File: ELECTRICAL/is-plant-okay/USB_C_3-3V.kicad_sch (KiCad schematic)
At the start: 0 parts

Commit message: feat: add usb and esd protection device
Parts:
- added C11: 4n7 1KV, symbol Device:C
- added J7: USB4085-GF-A_REVB, is-plant-okay-foot:GCT_USB4085-GF-A_REVB, symbol is-plant-okay-lib:USB4085-GF-A_REVB
- added R12: 1M, symbol Device:R
- added R13, R14: 5.1k, symbol Device:R
- added U6: USBLC6-2SC6, is-plant-okay-foot:SOT95P280X145-6N, symbol is-plant-okay-lib:USBLC6-2SC6
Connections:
- new net: J7.A5 (CC1), R14.2
- new net: J7.B5 (CC2), R13.2
- new net: C11.1, J7.S1 (SHELL), J7.S2 (SHELL__1), J7.S3 (SHELL__2), J7.S4 (SHELL__3), R12.1
- new net 5V: J7.A4 (VBUS), J7.A9 (VBUS__1), J7.B4 (VBUS__2), J7.B9 (VBUS__3), U6.5
- new net DATA_NEG: J7.A7 (DN1), J7.B7 (DN2), U6.3
- new net DATA_POS: J7.A6 (DP1), J7.B6 (DP2), U6.1
- new net GND: C11.2, J7.A1 (GND), J7.A12 (GND__1), J7.B1 (GND__2), J7.B12 (GND__3), R12.2, R13.1, R14.1, U6.2
- no-connect marks 0 -> 4

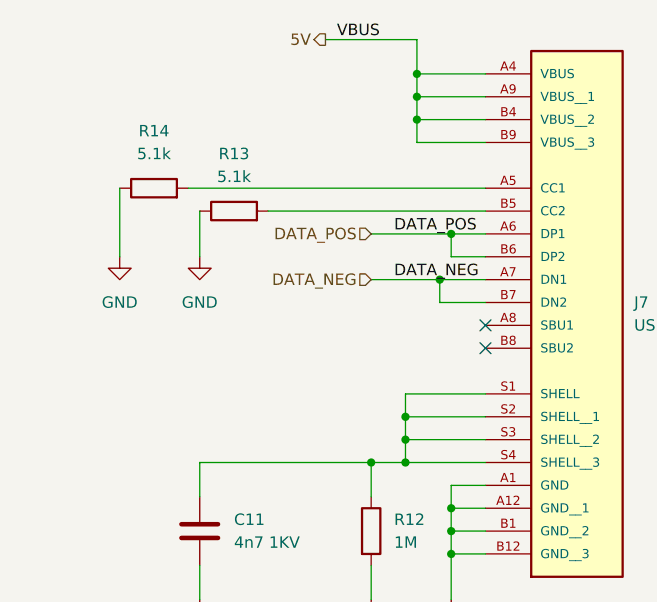
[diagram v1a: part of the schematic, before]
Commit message: feat: add ldo and power management IC
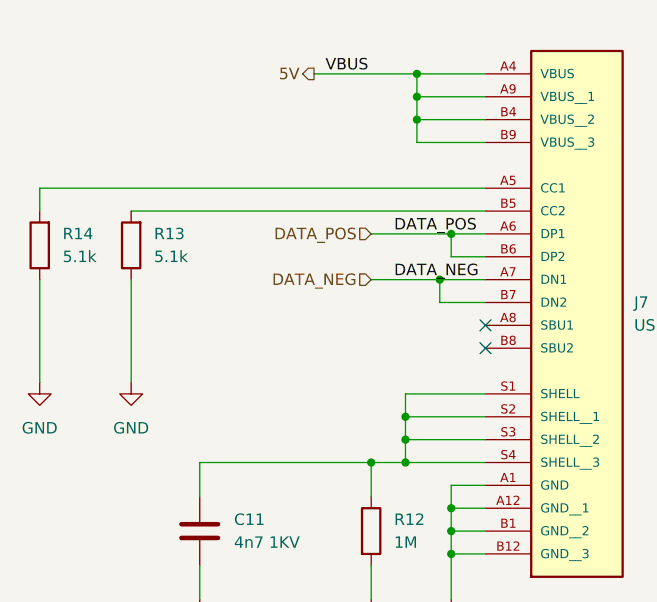
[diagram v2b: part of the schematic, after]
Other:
- moved on the sheet: R13, R14
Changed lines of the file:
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@@
 	(wire
 		(pts
-			(xy 99.06 80.01) (xy 99.06 85.09)
+			(xy 91.44 87.63) (xy 91.44 99.06)
 		)
 		(stroke
@@
 	(wire
 		(pts
-			(xy 97.79 77.47) (xy 130.81 77.47)
-		)
-		(stroke
-			(width 0)
-			(type default)
-		)
-	)
-	(wire
-		(pts
 			(xy 118.11 87.63) (xy 125.73 87.63)
 		)
@@
 	(wire
 		(pts
+			(xy 81.28 77.47) (xy 81.28 80.01)
+		)
+		(stroke
+			(width 0)
+			(type default)
+		)
+	)
+	(wire
+		(pts
 			(xy 127 118.11) (xy 127 123.19)
 		)
@@
 	(wire
 		(pts
-			(xy 106.68 80.01) (xy 130.81 80.01)
-		)
-		(stroke
-			(width 0)
-			(type default)
-		)
-	)
-	(wire
-		(pts
 			(xy 99.06 107.95) (xy 99.06 111.76)
 		)
@@
 	(wire
 		(pts
-			(xy 123.19 64.77) (xy 123.19 60.96)
-		)
-		(stroke
-			(width 0)
-			(type default)
-		)
-	)
-	(wire
-		(pts
 			(xy 127 110.49) (xy 127 113.03)
 		)
@@
 	(wire
 		(pts
-			(xy 113.03 60.96) (xy 123.19 60.96)
+			(xy 111.76 64.77) (xy 123.19 64.77)
 		)
 		(stroke
@@
 	(wire
 		(pts
+			(xy 81.28 77.47) (xy 130.81 77.47)
+		)
+		(stroke
+			(width 0)
+			(type default)
+		)
+	)
+	(wire
+		(pts
 			(xy 127 113.03) (xy 127 115.57)
 		)
@@
 	(wire
 		(pts
-			(xy 90.17 77.47) (xy 90.17 85.09)
-		)
-		(stroke
-			(width 0)
-			(type default)
-		)
-	)
-	(wire
-		(pts
 			(xy 123.19 69.85) (xy 130.81 69.85)
 		)
@@
 	(wire
 		(pts
+			(xy 81.28 87.63) (xy 81.28 99.06)
+		)
+		(stroke
+			(width 0)
+			(type default)
+		)
+	)
+	(wire
+		(pts
 			(xy 125.73 87.63) (xy 130.81 87.63)
 		)
@@
 	(wire
 		(pts
+			(xy 91.44 80.01) (xy 130.81 80.01)
+		)
+		(stroke
+			(width 0)
+			(type default)
+		)
+	)
+	(wire
+		(pts
 			(xy 121.92 100.33) (xy 121.92 102.87)
 		)
@@
 	)
 	(label "VBUS"
-		(at 114.3 60.96 0)
+		(at 113.03 64.77 0)
 		(effects
 			(font
@@
 	(hierarchical_label "5V"
 		(shape output)
-		(at 113.03 60.96 180)
+		(at 111.76 64.77 180)
 		(effects
 			(font
@@
 	(symbol
 		(lib_id "power:GND")
-		(at 90.17 85.09 0)
+		(at 81.28 99.06 0)
 		(unit 1)
 		(exclude_from_sim no)
@@
 		(fields_autoplaced yes)
 		(property "Reference" "#PWR036"
-			(at 90.17 91.44 0)
+			(at 81.28 105.41 0)
 			(effects
 				(font
@@
 		)
 		(property "Value" "GND"
-			(at 90.17 90.17 0)
+			(at 81.28 104.14 0)
 			(effects
 				(font
@@
 		)
 		(property "Footprint" ""
-			(at 90.17 85.09 0)
+			(at 81.28 99.06 0)
 			(effects
 				(font
@@
 		)
 		(property "Datasheet" ""
-			(at 90.17 85.09 0)
+			(at 81.28 99.06 0)
 			(effects
 				(font
@@
 		)
 		(property "Description" "Power symbol creates a global label with name \"GND\" , ground"
-			(at 90.17 85.09 0)
+			(at 81.28 99.06 0)
 			(effects
 				(font
@@
 	(symbol
 		(lib_id "Device:R")
-		(at 102.87 80.01 90)
+		(at 91.44 83.82 180)
 		(unit 1)
 		(exclude_from_sim no)
@@
 		(fields_autoplaced yes)
 		(property "Reference" "R13"
-			(at 102.87 73.66 90)
-			(effects
-				(font
-					(size 1.27 1.27)
-				)
+			(at 93.98 82.5499 0)
+			(effects
+				(font
+					(size 1.27 1.27)
+				)
+				(justify right)
 			)
 		)
 		(property "Value" "5.1k"
-			(at 102.87 76.2 90)
-			(effects
-				(font
-					(size 1.27 1.27)
-				)
+			(at 93.98 85.0899 0)
+			(effects
+				(font
+					(size 1.27 1.27)
+				)
+				(justify right)
 			)
 		)
 		(property "Footprint" ""
-			(at 102.87 81.788 90)
+			(at 93.218 83.82 90)
 			(effects
 				(font
@@
 		)
 		(property "Datasheet" "~"
-			(at 102.87 80.01 0)
+			(at 91.44 83.82 0)
 			(effects
 				(font
@@
 		)
 		(property "Description" "Resistor"
-			(at 102.87 80.01 0)
+			(at 91.44 83.82 0)
 			(effects
 				(font
@@
 	(symbol
 		(lib_id "power:GND")
-		(at 99.06 85.09 0)
+		(at 91.44 99.06 0)
 		(unit 1)
 		(exclude_from_sim no)
@@
 		(fields_autoplaced yes)
 		(property "Reference" "#PWR035"
-			(at 99.06 91.44 0)
+			(at 91.44 105.41 0)
 			(effects
 				(font
@@
 		)
 		(property "Value" "GND"
-			(at 99.06 90.17 0)
+			(at 91.44 104.14 0)
 			(effects
 				(font
@@
 		)
 		(property "Footprint" ""
-			(at 99.06 85.09 0)
+			(at 91.44 99.06 0)
 			(effects
 				(font
@@
 		)
 		(property "Datasheet" ""
-			(at 99.06 85.09 0)
+			(at 91.44 99.06 0)
 			(effects
 				(font
@@
 		)
 		(property "Description" "Power symbol creates a global label with name \"GND\" , ground"
-			(at 99.06 85.09 0)
+			(at 91.44 99.06 0)
 			(effects
 				(font
@@
 	(symbol
 		(lib_id "Device:R")
-		(at 93.98 77.47 90)
+		(at 81.28 83.82 180)
 		(unit 1)
 		(exclude_from_sim no)
@@
 		(fields_autoplaced yes)
 		(property "Reference" "R14"
-			(at 93.98 71.12 90)
-			(effects
-				(font
-					(size 1.27 1.27)
-				)
+			(at 83.82 82.5499 0)
+			(effects
+				(font
+					(size 1.27 1.27)
+				)
+				(justify right)
 			)
 		)
 		(property "Value" "5.1k"
-			(at 93.98 73.66 90)
-			(effects
-				(font
-					(size 1.27 1.27)
-				)
+			(at 83.82 85.0899 0)
+			(effects
+				(font
+					(size 1.27 1.27)
+				)
+				(justify right)
 			)
 		)
 		(property "Footprint" ""
-			(at 93.98 79.248 90)
+			(at 83.058 83.82 90)
 			(effects
 				(font
@@
 		)
 		(property "Datasheet" "~"
-			(at 93.98 77.47 0)
+			(at 81.28 83.82 0)
 			(effects
 				(font
@@
 		)
 		(property "Description" "Resistor"
-			(at 93.98 77.47 0)
-			(effects
-				(font
+			(at 81.28 83.82 0)
+			(effects
+				(font

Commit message: feat: add ldo and power management IC
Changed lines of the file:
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@@
+	)
+	(junction
+		(at 120.65 64.77)
+		(diameter 0)
+		(color 0 0 0 0)
 	)
 	(junction
@@
 	(junction
 		(at 123.19 67.31)
+		(diameter 0)
+		(color 0 0 0 0)
+	)
+	(junction
+		(at 127 125.73)
 		(diameter 0)
 		(color 0 0 0 0)
@@
 	(wire
 		(pts
+			(xy 120.65 64.77) (xy 123.19 64.77)
+		)
+		(stroke
+			(width 0)
+			(type default)
+		)
+	)
+	(wire
+		(pts
 			(xy 127 113.03) (xy 130.81 113.03)
 		)
@@
 	(wire
 		(pts
-			(xy 127 118.11) (xy 127 123.19)
+			(xy 127 118.11) (xy 127 125.73)
 		)
 		(stroke
@@
 	(wire
 		(pts
-			(xy 99.06 119.38) (xy 99.06 123.19)
+			(xy 99.06 119.38) (xy 99.06 127)
 		)
 		(stroke
@@
 	(wire
 		(pts
-			(xy 111.76 64.77) (xy 123.19 64.77)
+			(xy 111.76 64.77) (xy 120.65 64.77)
 		)
 		(stroke
@@
 	(wire
 		(pts
-			(xy 118.11 119.38) (xy 118.11 123.19)
+			(xy 118.11 119.38) (xy 118.11 127)
 		)
 		(stroke
@@
 		(pts
 			(xy 121.92 107.95) (xy 130.81 107.95)
+		)
+		(stroke
+			(width 0)
+			(type default)
+		)
+	)
+	(wire
+		(pts
+			(xy 127 125.73) (xy 127 127)
 		)
 		(stroke
@@
 	)
 	(symbol
+		(lib_id "power:PWR_FLAG")
+		(at 127 125.73 270)
+		(unit 1)
+		(exclude_from_sim no)
+		(in_bom yes)
+		(on_board yes)
+		(dnp no)
+		(fields_autoplaced yes)
+		(property "Reference" "#FLG02"
+			(at 128.905 125.73 0)
+			(effects
+				(font
+					(size 1.27 1.27)
+				)
+				(hide yes)
+			)
+		)
+		(property "Value" "PWR_FLAG"
+			(at 130.81 125.7299 90)
+			(effects
+				(font
+					(size 1.27 1.27)
+				)
+				(justify left)
+			)
+		)
+		(property "Footprint" ""
+			(at 127 125.73 0)
+			(effects
+				(font
+					(size 1.27 1.27)
+				)
+				(hide yes)
+			)
+		)
+		(property "Datasheet" "~"
+			(at 127 125.73 0)
+			(effects
+				(font
+					(size 1.27 1.27)
+				)
+				(hide yes)
+			)
+		)
+		(property "Description" "Special symbol for telling ERC where power comes from"
+			(at 127 125.73 0)
+			(effects
+				(font
+					(size 1.27 1.27)
+				)
+				(hide yes)
+			)
+		)
+		(pin "1"
+		)
+		(instances
+			(project "is-plant-okay"
+				(path "/ac51c2f9-77a4-4b89-b63f-6e0ba02b1e45/67cc056f-c5be-4963-a238-c27ae3faab2e"
+					(reference "#FLG02")
+					(unit 1)
+				)
+			)
+		)
+	)
+	(symbol
 		(lib_id "power:GND")
-		(at 99.06 123.19 0)
+		(at 99.06 127 0)
 		(unit 1)
 		(exclude_from_sim no)
@@
 		(fields_autoplaced yes)
 		(property "Reference" "#PWR034"
-			(at 99.06 129.54 0)
+			(at 99.06 133.35 0)
 			(effects
 				(font
@@
 		)
 		(property "Value" "GND"
-			(at 99.06 128.27 0)
+			(at 99.06 132.08 0)
 			(effects
 				(font
@@
 		)
 		(property "Footprint" ""
-			(at 99.06 123.19 0)
+			(at 99.06 127 0)
 			(effects
 				(font
@@
 		)
 		(property "Datasheet" ""
-			(at 99.06 123.19 0)
+			(at 99.06 127 0)
 			(effects
 				(font
@@
 		)
 		(property "Description" "Power symbol creates a global label with name \"GND\" , ground"
-			(at 99.06 123.19 0)
+			(at 99.06 127 0)
 			(effects
 				(font
@@
 				(path "/ac51c2f9-77a4-4b89-b63f-6e0ba02b1e45/67cc056f-c5be-4963-a238-c27ae3faab2e"
 					(reference "#PWR034")
+					(unit 1)
+				)
+			)
+		)
+	)
+	(symbol
+		(lib_id "power:PWR_FLAG")
+		(at 120.65 64.77 0)
+		(unit 1)
+		(exclude_from_sim no)
+		(in_bom yes)
+		(on_board yes)
+		(dnp no)
+		(fields_autoplaced yes)
+		(property "Reference" "#FLG01"
+			(at 120.65 62.865 0)
+			(effects
+				(font
+					(size 1.27 1.27)
+				)
+				(hide yes)
+			)
+		)
+		(property "Value" "PWR_FLAG"
+			(at 120.65 59.69 0)
+			(effects
+				(font
+					(size 1.27 1.27)
+				)
+			)
+		)
+		(property "Footprint" ""
+			(at 120.65 64.77 0)
+			(effects
+				(font
+					(size 1.27 1.27)
+				)
+				(hide yes)
+			)
+		)
+		(property "Datasheet" "~"
+			(at 120.65 64.77 0)
+			(effects
+				(font
+					(size 1.27 1.27)
+				)
+				(hide yes)
+			)
+		)
+		(property "Description" "Special symbol for telling ERC where power comes from"
+			(at 120.65 64.77 0)
+			(effects
+				(font
+					(size 1.27 1.27)
+				)
+				(hide yes)
+			)
+		)
+		(pin "1"
+		)
+		(instances
+			(project ""
+				(path "/ac51c2f9-77a4-4b89-b63f-6e0ba02b1e45/67cc056f-c5be-4963-a238-c27ae3faab2e"
+					(reference "#FLG01")
 					(unit 1)
 				)
@@
 	(symbol
 		(lib_id "power:GND")
-		(at 127 123.19 0)
+		(at 127 127 0)
 		(unit 1)
 		(exclude_from_sim no)
@@
 		(fields_autoplaced yes)
 		(property "Reference" "#PWR032"
-			(at 127 129.54 0)
+			(at 127 133.35 0)
 			(effects
 				(font
@@
 		)
 		(property "Value" "GND"
-			(at 127 128.27 0)
+			(at 127 132.08 0)
 			(effects
 				(font
@@
 		)
 		(property "Footprint" ""
-			(at 127 123.19 0)
+			(at 127 127 0)
 			(effects
 				(font
@@
 		)
 		(property "Datasheet" ""
-			(at 127 123.19 0)
+			(at 127 127 0)
 			(effects
 				(font
@@
 		)
 		(property "Description" "Power symbol creates a global label with name \"GND\" , ground"
-			(at 127 123.19 0)
+			(at 127 127 0)
 			(effects
 				(font
@@
 	(symbol
 		(lib_id "power:GND")
-		(at 118.11 123.19 0)
+		(at 118.11 127 0)
 		(unit 1)
 		(exclude_from_sim no)
@@
 		(fields_autoplaced yes)
 		(property "Reference" "#PWR033"
-			(at 118.11 129.54 0)
+			(at 118.11 133.35 0)
 			(effects
 				(font
@@
 		)
 		(property "Value" "GND"
-			(at 118.11 128.27 0)
+			(at 118.11 132.08 0)
 			(effects
 				(font
@@
 		)
 		(property "Footprint" ""
-			(at 118.11 123.19 0)
+			(at 118.11 127 0)
 			(effects
 				(font
@@
 		)
 		(property "Datasheet" ""
-			(at 118.11 123.19 0)
+			(at 118.11 127 0)
 			(effects
 				(font
@@
 		)
 		(property "Description" "Power symbol creates a global label with name \"GND\" , ground"
-			(at 118.11 123.19 0)
-			(effects
-				(font
+			(at 118.11 127 0)
+			(effects
+				(font

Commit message: feat: add pins for bootloader programmer
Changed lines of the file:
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@@
 	)
 	(hierarchical_label "DATA_NEG"
-		(shape input)
+		(shape output)
 		(at 118.11 87.63 180)
 		(effects
@@
 	)
 	(hierarchical_label "DATA_POS"
-		(shape input)
+		(shape output)
 		(at 118.11 82.55 180)
 		(effects

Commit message: feat: finished schematics
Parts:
- added TP8: USB_5V_TP, TestPoint:TestPoint_Keystone_5000-5004_Miniature, symbol Connector:TestPoint
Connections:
- net 5V: now also TP8.1
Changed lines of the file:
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@@
+	)
+	(junction
+		(at 96.52 64.77)
+		(diameter 0)
+		(color 0 0 0 0)
 	)
 	(junction
@@
 	(wire
 		(pts
+			(xy 96.52 64.77) (xy 120.65 64.77)
+		)
+		(stroke
+			(width 0)
+			(type default)
+		)
+	)
+	(wire
+		(pts
 			(xy 127 118.11) (xy 127 125.73)
 		)
@@
 	(wire
 		(pts
-			(xy 111.76 64.77) (xy 120.65 64.77)
+			(xy 93.98 64.77) (xy 96.52 64.77)
 		)
 		(stroke
@@
 	(hierarchical_label "5V"
 		(shape output)
-		(at 111.76 64.77 180)
+		(at 93.98 64.77 180)
 		(effects
 			(font
@@
 					(unit 1)
 				)
+			)
+		)
+	)
+	(symbol
+		(lib_id "Connector:TestPoint")
+		(at 96.52 64.77 0)
+		(unit 1)
+		(exclude_from_sim no)
+		(in_bom yes)
+		(on_board yes)
+		(dnp no)
+		(fields_autoplaced yes)
+		(property "Reference" "TP8"
+			(at 99.06 60.1979 0)
+			(effects
+				(font
+					(size 1.27 1.27)
+				)
+				(justify left)
+			)
+		)
+		(property "Value" "USB_5V_TP"
+			(at 99.06 62.7379 0)
+			(effects
+				(font
+					(size 1.27 1.27)
+				)
+				(justify left)
+			)
+		)
+		(property "Footprint" "TestPoint:TestPoint_Keystone_5000-5004_Miniature"
+			(at 101.6 64.77 0)
+			(effects
+				(font
+					(size 1.27 1.27)
+				)
+				(hide yes)
+			)
+		)
+		(property "Datasheet" "~"
+			(at 101.6 64.77 0)
+			(effects
+				(font
+					(size 1.27 1.27)
+				)
+				(hide yes)
+			)
+		)
+		(property "Description" "test point"
+			(at 96.52 64.77 0)
+			(effects
+				(font
+					(size 1.27 1.27)
+				)
+				(hide yes)
+			)
+		)
+		(pin "1"
+		)
+		(instances
+			(project "is-plant-okay"
+				(path "/ac51c2f9-77a4-4b89-b63f-6e0ba02b1e45/67cc056f-c5be-4963-a238-c27ae3faab2e"
+					(reference "TP8")
+					(unit 1)
+				)

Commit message: feat: add resistor footprint
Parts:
- removed R12: 1M, symbol Device:R
- removed R13, R14: 5.1k, symbol Device:R
- added R1, R2: 5.1k, is-plant-okay-foot:RC0805JR-075K1L, symbol Device:R
- added R3: 10K, is-plant-okay-foot:RC0805FR-7W10KL, symbol Device:R
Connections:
- net GND: now also R1.1, R2.1, R3.2
- net at J7.A5 (CC1): now also R1.2
- net at J7.B5 (CC2): now also R2.2
- net at C11.1, J7.S1 (SHELL), J7.S2 (SHELL__1)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: now also R3.1
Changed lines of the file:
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@@
+	)
+	(symbol
+		(lib_id "Device:R")
+		(at 118.11 115.57 0)
+		(unit 1)
+		(exclude_from_sim no)
+		(in_bom yes)
+		(on_board yes)
+		(dnp no)
+		(fields_autoplaced yes)
+		(property "Reference" "R3"
+			(at 120.65 114.2999 0)
+			(effects
+				(font
+					(size 1.27 1.27)
+				)
+				(justify left)
+			)
+		)
+		(property "Value" "10K"
+			(at 120.65 116.8399 0)
+			(effects
+				(font
+					(size 1.27 1.27)
+				)
+				(justify left)
+			)
+		)
+		(property "Footprint" "is-plant-okay-foot:RC0805FR-7W10KL"
+			(at 116.332 115.57 90)
+			(effects
+				(font
+					(size 1.27 1.27)
+				)
+				(hide yes)
+			)
+		)
+		(property "Datasheet" "~https://www.yageogroup.com/content/datasheet/asset/file/PYU-RC_GROUP_51_ROHS_L"
+			(at 118.11 115.57 0)
+			(effects
+				(font
+					(size 1.27 1.27)
+				)
+				(hide yes)
+			)
+		)
+		(property "Description" "RES 10K OHM 1% 1/4W 0805"
+			(at 118.11 115.57 0)
+			(effects
+				(font
+					(size 1.27 1.27)
+				)
+				(hide yes)
+			)
+		)
+		(property "MFG PART #" "RC0805FR-7W10KL"
+			(at 118.11 115.57 0)
+			(effects
+				(font
+					(size 1.27 1.27)
+				)
+				(hide yes)
+			)
+		)
+		(property "TYPE" "SMD"
+			(at 118.11 115.57 0)
+			(effects
+				(font
+					(size 1.27 1.27)
+				)
+				(hide yes)
+			)
+		)
+		(property "PACKAGE" "0805"
+			(at 118.11 115.57 0)
+			(effects
+				(font
+					(size 1.27 1.27)
+				)
+				(hide yes)
+			)
+		)
+		(pin "1"
+		)
+		(pin "2"
+		)
+		(instances
+			(project "is-plant-okay"
+				(path "/ac51c2f9-77a4-4b89-b63f-6e0ba02b1e45/67cc056f-c5be-4963-a238-c27ae3faab2e"
+					(reference "R3")
+					(unit 1)
+				)
+			)
+		)
 	)
 	(symbol
@@
 	)
 	(symbol
+		(lib_id "Device:R")
+		(at 91.44 83.82 180)
+		(unit 1)
+		(exclude_from_sim no)
+		(in_bom yes)
+		(on_board yes)
+		(dnp no)
+		(fields_autoplaced yes)
+		(property "Reference" "R2"
+			(at 93.98 82.5499 0)
+			(effects
+				(font
+					(size 1.27 1.27)
+				)
+				(justify right)
+			)
+		)
+		(property "Value" "5.1k"
+			(at 93.98 85.0899 0)
+			(effects
+				(font
+					(size 1.27 1.27)
+				)
+				(justify right)
+			)
+		)
+		(property "Footprint" "is-plant-okay-foot:RC0805JR-075K1L"
+			(at 93.218 83.82 90)
+			(effects
+				(font
+					(size 1.27 1.27)
+				)
+				(hide yes)
+			)
+		)
+		(property "Datasheet" "https://www.yageogroup.com/content/datasheet/asset/file/PYU-RC_GROUP_51_ROHS_L"
+			(at 91.44 83.82 0)
+			(effects
+				(font
+					(size 1.27 1.27)
+				)
+				(hide yes)
+			)
+		)
+		(property "Description" "RES 5.1K OHM 5% 1/8W 0805"
+			(at 91.44 83.82 0)
+			(effects
+				(font
+					(size 1.27 1.27)
+				)
+				(hide yes)
+			)
+		)
+		(property "MFG PART #" "RC0805JR-075K1L"
+			(at 91.44 83.82 0)
+			(effects
+				(font
+					(size 1.27 1.27)
+				)
+				(hide yes)
+			)
+		)
+		(property "TYPE" "SMD"
+			(at 91.44 83.82 0)
+			(effects
+				(font
+					(size 1.27 1.27)
+				)
+				(hide yes)
+			)
+		)
+		(property "PACKAGE" "0805"
+			(at 91.44 83.82 0)
+			(effects
+				(font
+					(size 1.27 1.27)
+				)
+				(hide yes)
+			)
+		)
+		(pin "1"
+		)
+		(pin "2"
+		)
+		(instances
+			(project "is-plant-okay"
+				(path "/ac51c2f9-77a4-4b89-b63f-6e0ba02b1e45/67cc056f-c5be-4963-a238-c27ae3faab2e"
+					(reference "R2")
+					(unit 1)
+				)
+			)
+		)
+	)
+	(symbol
 		(lib_id "power:GND")
 		(at 81.28 99.06 0)
@@
 	)
 	(symbol
-		(lib_id "Device:R")
-		(at 91.44 83.82 180)
-		(unit 1)
-		(exclude_from_sim no)
-		(in_bom yes)
-		(on_board yes)
-		(dnp no)
-		(fields_autoplaced yes)
-		(property "Reference" "R13"
-			(at 93.98 82.5499 0)
-			(effects
-				(font
-					(size 1.27 1.27)
-				)
-				(justify right)
-			)
-		)
-		(property "Value" "5.1k"
-			(at 93.98 85.0899 0)
-			(effects
-				(font
-					(size 1.27 1.27)
-				)
-				(justify right)
-			)
-		)
-		(property "Footprint" ""
-			(at 93.218 83.82 90)
-			(effects
-				(font
-					(size 1.27 1.27)
-				)
-				(hide yes)
-			)
-		)
-		(property "Datasheet" "~"
-			(at 91.44 83.82 0)
-			(effects
-				(font
-					(size 1.27 1.27)
-				)
-				(hide yes)
-			)
-		)
-		(property "Description" "Resistor"
-			(at 91.44 83.82 0)
-			(effects
-				(font
-					(size 1.27 1.27)
-				)
-				(hide yes)
-			)
-		)
-		(pin "1"
-		)
-		(pin "2"
-		)
-		(instances
-			(project "is-plant-okay"
-				(path "/ac51c2f9-77a4-4b89-b63f-6e0ba02b1e45/67cc056f-c5be-4963-a238-c27ae3faab2e"
-					(reference "R13")
-					(unit 1)
-				)
-			)
-		)
-	)
-	(symbol
 		(lib_id "power:GND")
 		(at 91.44 99.06 0)
@@
 	(symbol
 		(lib_id "Device:R")
-		(at 118.11 115.57 0)
-		(unit 1)
-		(exclude_from_sim no)
-		(in_bom yes)
-		(on_board yes)
-		(dnp no)
-		(fields_autoplaced yes)
-		(property "Reference" "R12"
-			(at 120.65 114.2999 0)
-			(effects
-				(font
-					(size 1.27 1.27)
-				)
-				(justify left)
-			)
-		)
-		(property "Value" "1M"
-			(at 120.65 116.8399 0)
-			(effects
-				(font
-					(size 1.27 1.27)
-				)
-				(justify left)
-			)
-		)
-		(property "Footprint" ""
-			(at 116.332 115.57 90)
-			(effects
-				(font
-					(size 1.27 1.27)
-				)
-				(hide yes)
-			)
-		)
-		(property "Datasheet" "~"
-			(at 118.11 115.57 0)
-			(effects
-				(font
-					(size 1.27 1.27)
-				)
-				(hide yes)
-			)
-		)
-		(property "Description" "Resistor"
-			(at 118.11 115.57 0)
-			(effects
-				(font
-					(size 1.27 1.27)
-				)
-				(hide yes)
-			)
-		)
-		(pin "1"
-		)
-		(pin "2"
-		)
-		(instances
-			(project ""
-				(path "/ac51c2f9-77a4-4b89-b63f-6e0ba02b1e45/67cc056f-c5be-4963-a238-c27ae3faab2e"
-					(reference "R12")
-					(unit 1)
-				)
-			)
-		)
-	)
-	(symbol
-		(lib_id "Device:R")
 		(at 81.28 83.82 180)
 		(unit 1)
@@
 		(dnp no)
 		(fields_autoplaced yes)
-		(property "Reference" "R14"
+		(property "Reference" "R1"
 			(at 83.82 82.5499 0)
 			(effects
@@
 			)
 		)
-		(property "Footprint" ""
+		(property "Footprint" "is-plant-okay-foot:RC0805JR-075K1L"
 			(at 83.058 83.82 90)
 			(effects
@@
 			)
 		)
-		(property "Datasheet" "~"
+		(property "Datasheet" "https://www.yageogroup.com/content/datasheet/asset/file/PYU-RC_GROUP_51_ROHS_L"
 			(at 81.28 83.82 0)
 			(effects
@@
 			)
 		)
-		(property "Description" "Resistor"
+		(property "Description" "RES 5.1K OHM 5% 1/8W 0805"
 			(at 81.28 83.82 0)
 			(effects
@@
 			)
 		)
+		(property "MFG PART #" "RC0805JR-075K1L"
+			(at 81.28 83.82 0)
+			(effects
+				(font
+					(size 1.27 1.27)
+				)
+				(hide yes)
+			)
+		)
+		(property "TYPE" "SMD"
+			(at 81.28 83.82 0)
+			(effects
+				(font
+					(size 1.27 1.27)
+				)
+				(hide yes)
+			)
+		)
+		(property "PACKAGE" "0805"
+			(at 81.28 83.82 0)
+			(effects
+				(font
+					(size 1.27 1.27)
+				)
+				(hide yes)
+			)
+		)
 		(pin "1"
 		)
@@
 			(project "is-plant-okay"
 				(path "/ac51c2f9-77a4-4b89-b63f-6e0ba02b1e45/67cc056f-c5be-4963-a238-c27ae3faab2e"
-					(reference "R14")
-					(unit 1)
-				)
+					(reference "R1")
+					(unit 1)
+				)
